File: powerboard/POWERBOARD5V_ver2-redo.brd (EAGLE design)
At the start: 42 x 70 mm, 37 parts, among them IC1 TPS5420, IC2 TPS5420

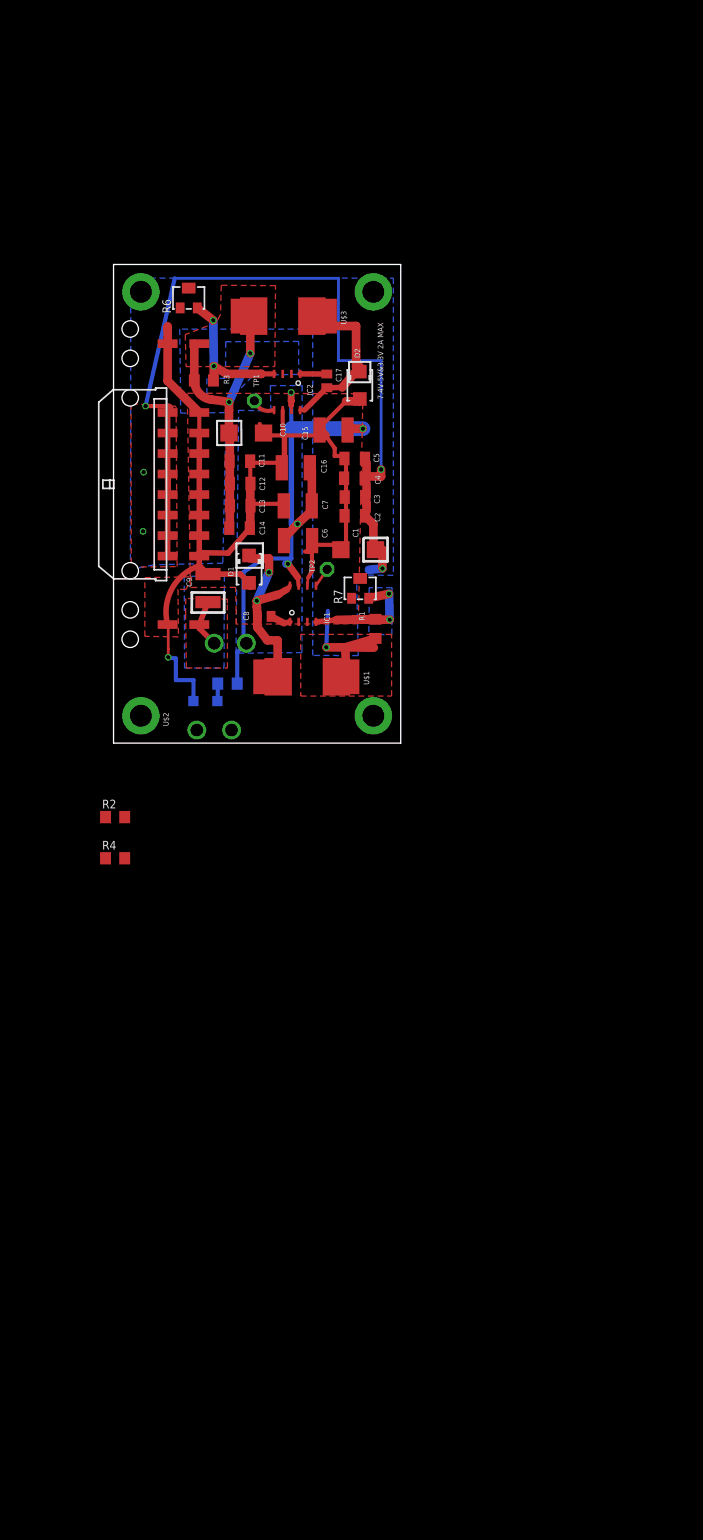
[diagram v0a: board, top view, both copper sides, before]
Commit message: Added the 6volt rail to schematic. Board not done.
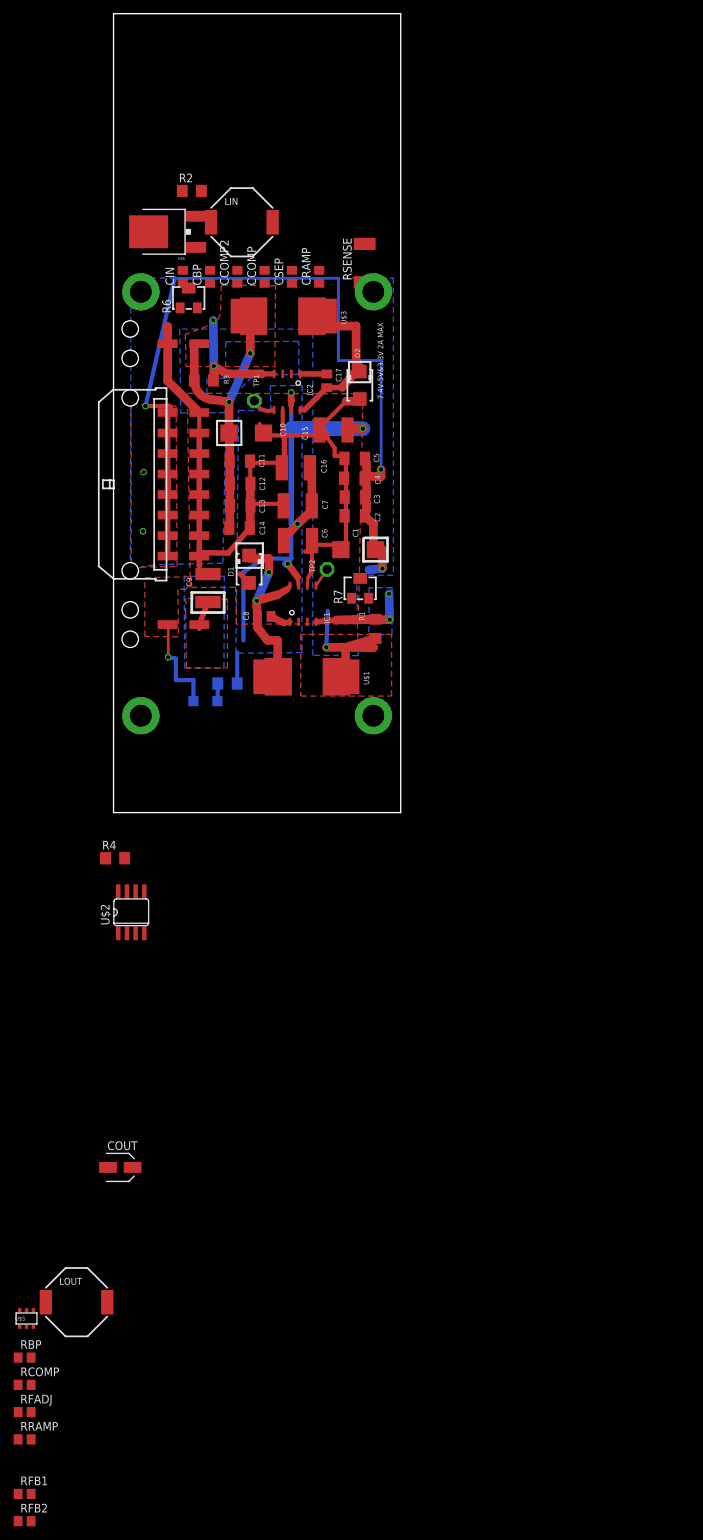
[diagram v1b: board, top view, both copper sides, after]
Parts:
- added CBP: 100nF, rcl:C0805
- added CCOMP: 120nF, rcl:C0805
- added CCOMP2: 510pF, rcl:C0805
- added CIN: 22uF, rcl:C0805
- added COUT: 56uF, rcl:SANYO-OSCON_SMD_A5
- added CRAMP: 750pF, rcl:C0805
- added CSEP: 2.2uF, rcl:C0805
- added LIN: 6.2uH, SparkFun-Passives:SRU1038
- added LOUT: 15uH, SparkFun-Passives:SRU1038
- added RBP: 20.0, rcl:R0805
- added RCOMP: 1.47k, rcl:R0805
- added RFADJ: 34.8k, rcl:R0805
- added RFB1: 10k, rcl:R0805
- added RFB2: 37.4k, rcl:R0805
- added RRAMP: 100.0, rcl:R0805
- added RSENSE: 0.016, rcl:R2512
- added U$5: P-CHANNEL20V(D-S)MOSFET, ngohara_parts:TSOP-6
- added U$6: DPAK_DIODE, ngohara_parts:DPAK
- U$2: value 90701WESWITCHDEV -> LM3488; device daniel:9070-1W-ESWITCH -> 40xx:SO08
- moved R2 92.3 mm to (11.5, 80.7)
- moved U$2 29.3 mm to (2.59, -24.7), turned to 0 degrees
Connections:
- net N$1 renamed 5V
- net N$9 renamed 3_3V
- removed net N$3: C15.1, C16.1, C6.1, C7.1, IC1.7, IC2.7, R5.1, U$2.1
- new net FB: RFB1.1, RFB2.2, U$2.3
- new net N$1: CCOMP.1, RCOMP.1
- new net N$20: RFADJ.2, U$2.7
- new net N$21: CRAMP.1, RRAMP.2, U$2.1
- new net N$22: RRAMP.1, RSENSE.2, U$5.P$1, U$5.P$2, U$5.P$5, U$5.P$6
- new net N$23: U$2.6, U$5.P$3
- new net N$24: CSEP.1, LIN.2, U$5.P$4
- new net N$25: CSEP.2, LOUT.1, U$6.1, U$6.3
- new net N$26: COUT.+, RFB2.1, U$6.4
- new net N$9: CBP.1, RBP.1, U$2.8
- new net V_BATT: C15.1, C16.1, C6.1, C7.1, C9.1, CIN.1, IC1.7, IC2.7, LIN.1, R5.1, RBP.2, X4.P$2
- net GND: now also CBP.2, CCOMP.2, CCOMP2.2, CIN.2, COUT.-, CRAMP.2, LOUT.2, RFADJ.1, RFB1.2, RSENSE.1, U$2.4, U$2.5
- net N$12: now also R6.2; no longer R6.3
- net N$5: now also R7.2; no longer R7.3
- net N$7: now also CCOMP2.1, RCOMP.2; no longer C9.1, X4.P$2
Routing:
- net V_BATT: track 0.00 -> 84.1 mm, vias 0 -> 4
- net N$3: track 82.0 -> 0.00 mm, vias 4 -> 0
- net GND: track 161.4 -> 144.8 mm
- net N$7: track 7.15 -> 0.00 mm
- net N$5: track 20.7 -> 17.7 mm
- net N$12: track 21.1 -> 18.1 mm
- added copper zone on layer 1, net V_BATT
- added copper zone on layer 16, net V_BATT
- removed copper zone on layer 1, net N$7
- removed copper zone on layer 16, net N$7
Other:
- board size 42 x 70 mm -> 42 x 116.8 mm

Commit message: Flipped board on side to fit within EagleLite's size limits
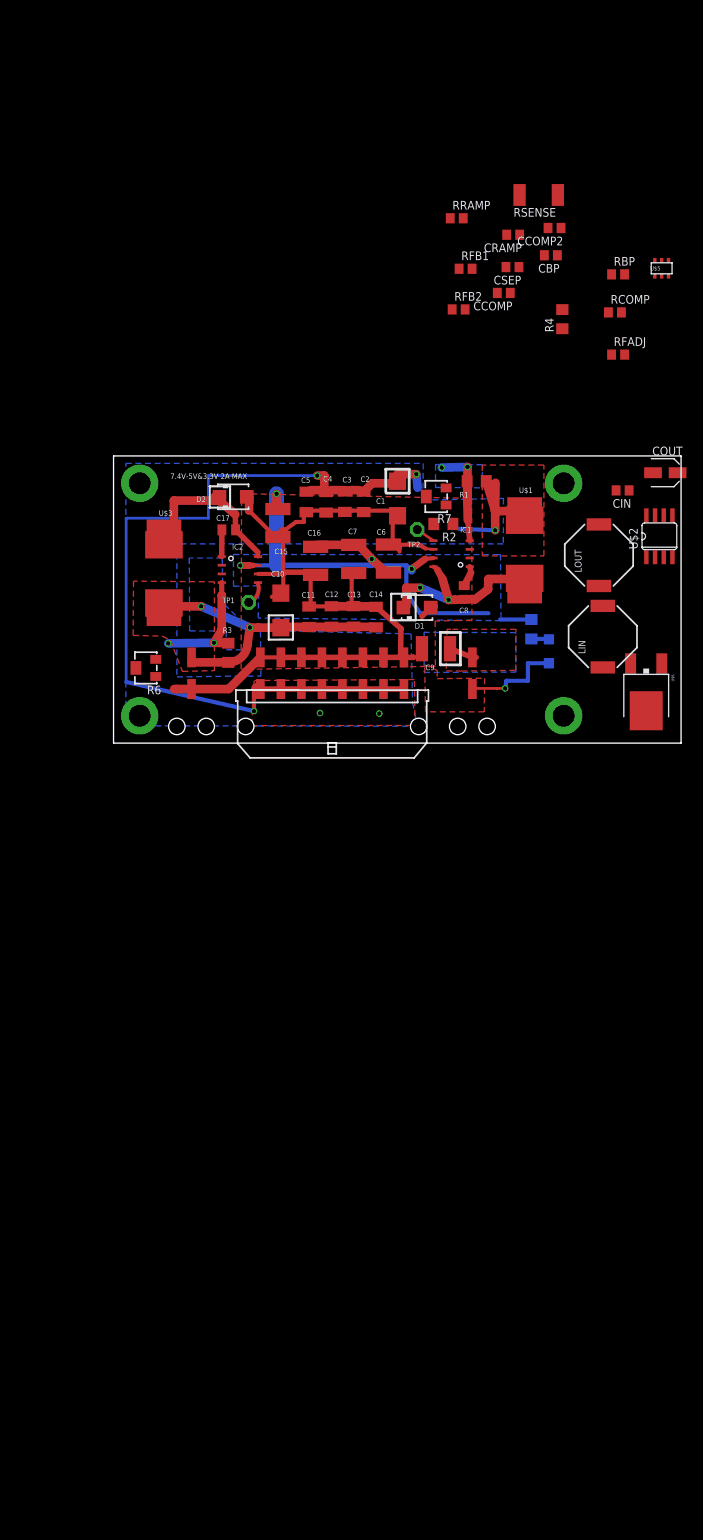
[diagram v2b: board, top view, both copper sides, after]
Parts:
- R2, R4: value 10.0k -> (none)
- moved RFB1 190.4 mm to (51.5, 69.4)
- moved RRAMP 189.4 mm to (50.2, 76.8)
- moved RFB2 188.2 mm to (50.5, 63.4)
- moved RBP 180.6 mm to (73.8, 68.6)
- moved U$5 179.5 mm to (80.2, 69.4)
- moved RCOMP 179.0 mm to (73.3, 63.0)
- moved RFADJ 177.3 mm to (73.8, 56.8)
- moved LOUT 133.3 mm to (71.0, 27.5), turned to 90 degrees
- moved COUT 129.1 mm to (80.7, 39.5)
- moved R4 102.4 mm to (65.6, 62.0), turned to 90 degrees
- moved U$6 98.7 mm to (77.9, 6.32), turned to 180 degrees
- moved U$2 94.8 mm to (79.8, 30.3)
- moved LIN 80.4 mm to (71.6, 15.6), turned to 90 degrees
- moved CIN 71.5 mm to (74.4, 37.0), turned to 180 degrees
- moved R2 61.0 mm to (48.2, 32.1), turned to 180 degrees
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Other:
- board size 42 x 116.8 mm -> 83 x 42 mm

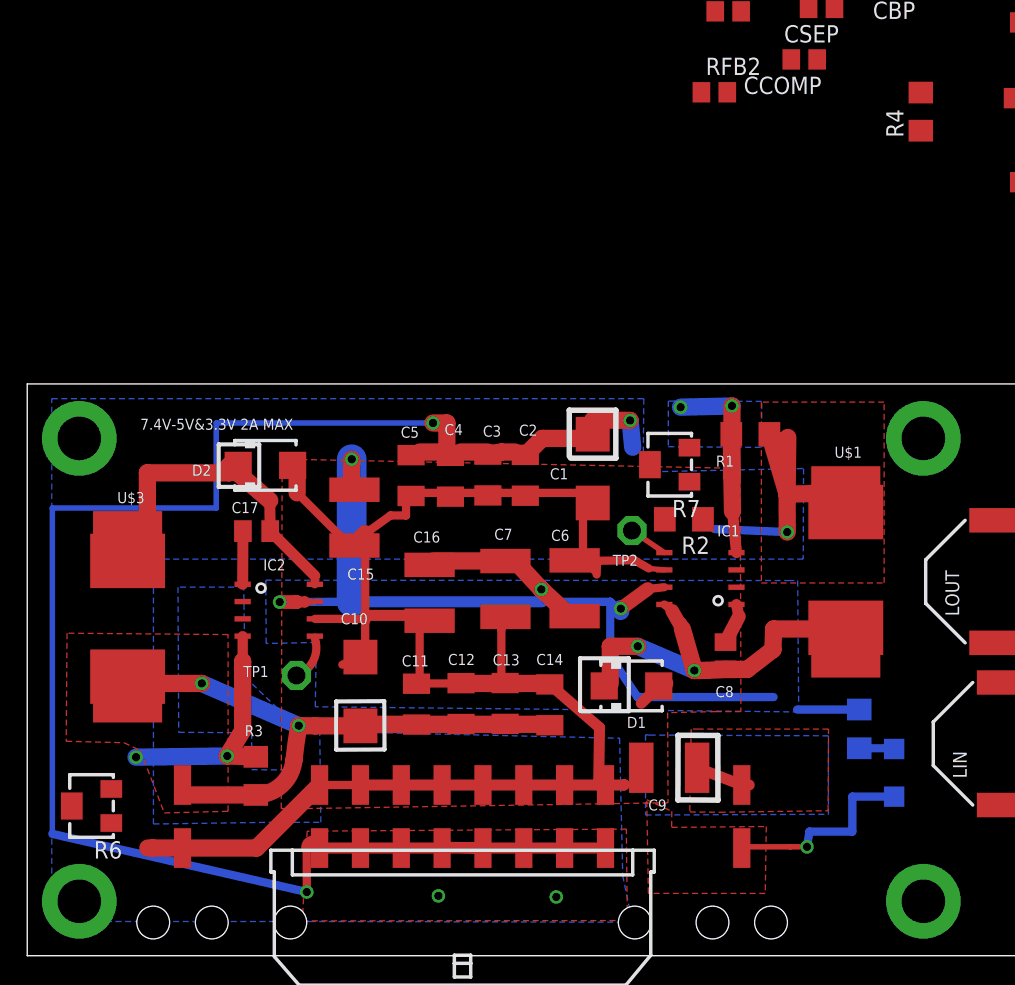
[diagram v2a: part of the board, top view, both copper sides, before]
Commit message: Deleted TP1 and TP2 (test points) because they seem useless
-Moved parts around to reduce footprint
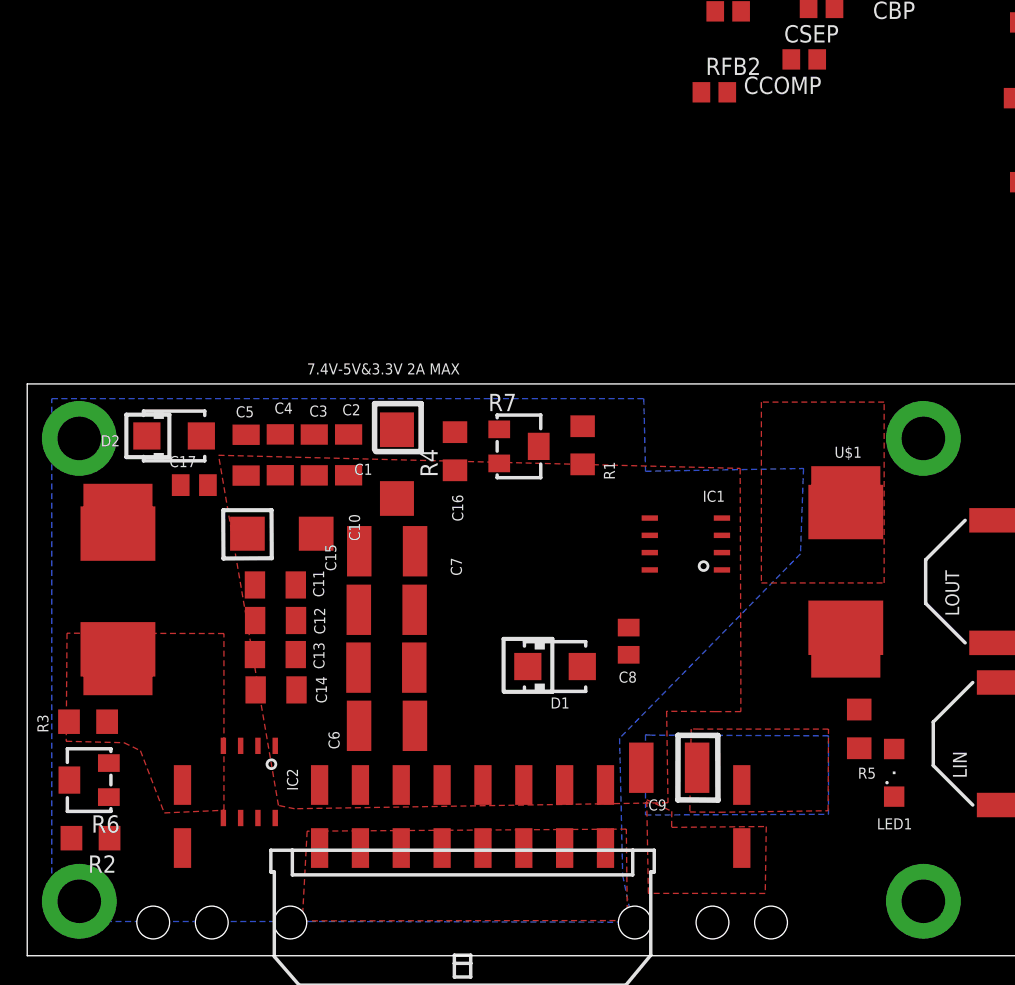
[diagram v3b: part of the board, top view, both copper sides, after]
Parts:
- removed TP1, TP2: PTR1PAD1-13, testpad:P1-13
- moved R2 49.5 mm to (4.65, 8.64)
- moved R4 42.3 mm to (31.4, 37.1)
- moved C14 20.1 mm to (18.3, 19.5), turned to 0 degrees
- moved C13 17.3 mm to (18.2, 22.1), turned to 0 degrees
- moved IC2 17.2 mm to (18.8, 10.8), turned to 180 degrees
- moved C6 17.1 mm to (26.4, 16.9), turned to 180 degrees
- moved C12 14.9 mm to (18.2, 24.6), turned to 0 degrees
- moved C1 14.4 mm to (27.2, 36.1)
- moved C11 13.6 mm to (18.2, 27.2), turned to 0 degrees
- moved C2 13.1 mm to (23.6, 36.8)
- moved C10 12.9 mm to (18.7, 31.0), turned to 180 degrees
- moved R3 12.9 mm to (4.47, 17.2), turned to 0 degrees
- moved C3 12.8 mm to (21.1, 36.8)
- moved C4 12.6 mm to (18.6, 36.8)
- moved R1 12.3 mm to (40.8, 37.5), turned to 90 degrees
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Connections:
- removed net N$4: IC2.5, TP1.TP
- removed net N$8: IC1.5, TP2.TP
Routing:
- net 5V: track 158.0 -> 0.00 mm, vias 6 -> 0
- net GND: track 144.8 -> 0.00 mm, vias 1 -> 0
- net V_BATT: track 84.1 -> 0.00 mm, vias 4 -> 0
- net 3_3V: track 46.3 -> 0.00 mm, vias 2 -> 0
- net N$6: track 32.5 -> 0.00 mm, vias 2 -> 0
- net N$13: track 29.4 -> 0.00 mm
- net N$12: track 18.1 -> 0.00 mm, vias 2 -> 0
- net N$5: track 17.7 -> 0.00 mm, vias 2 -> 0
- net N$10: track 3.91 -> 0.00 mm
- net N$4: track 3.20 -> 0.00 mm
- net N$2: track 3.02 -> 0.00 mm
- net N$8: track 2.88 -> 0.00 mm
- net N$17: track 2.59 -> 0.00 mm
- removed copper zone on layer 16, net 3_3V
- removed copper zone on layer 16, net N$3
- removed copper zone on layer 16, net N$5

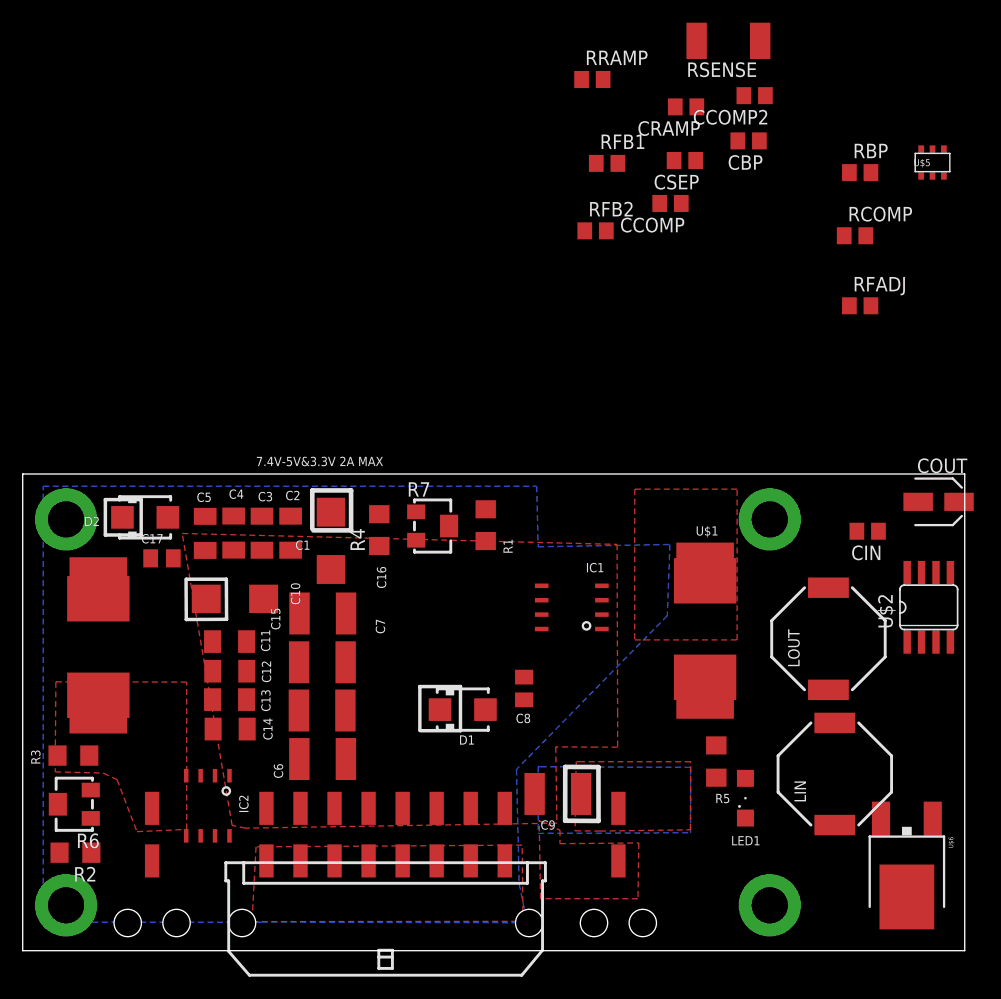
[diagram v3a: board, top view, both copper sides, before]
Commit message: Finished layout of power board with 6V.
-Does not include new connectors for 3.3 and 5v rail yet
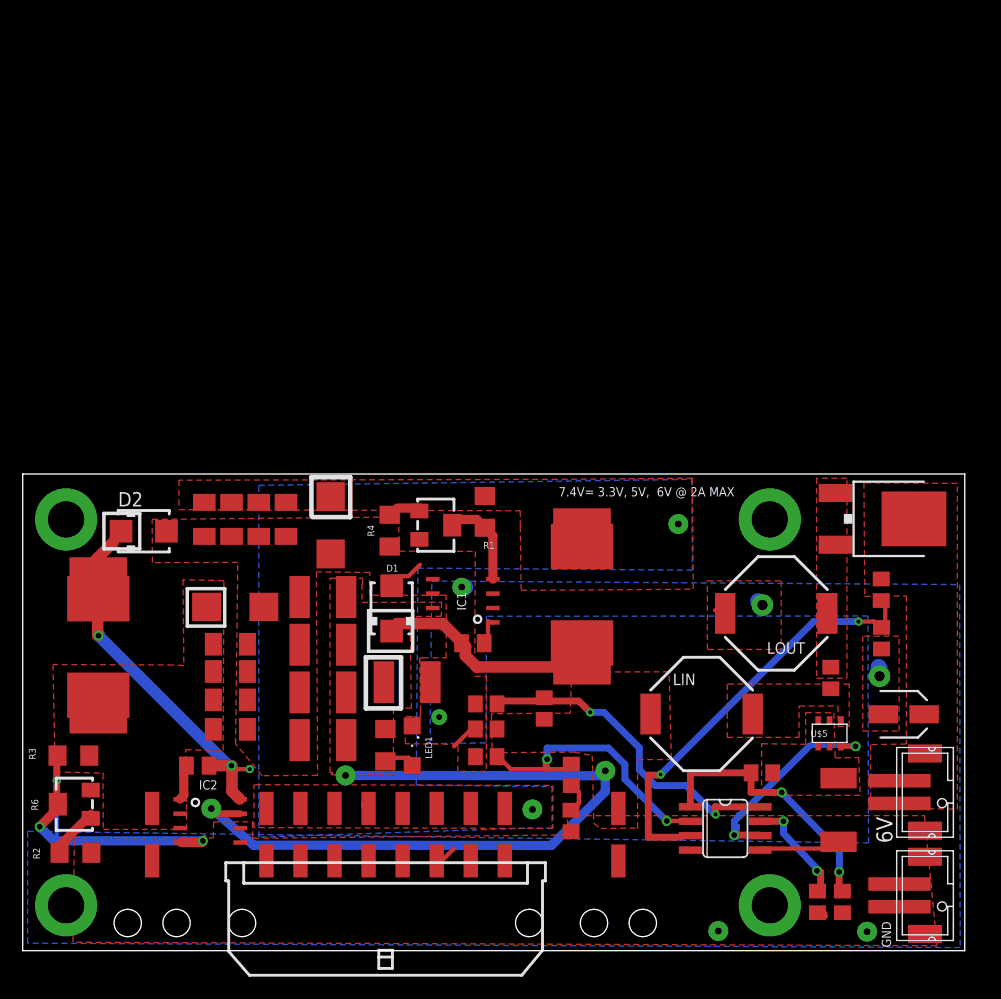
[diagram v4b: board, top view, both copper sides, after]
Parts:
- added U$4, U$7: JST-PH2-SMD, jst-ph:JST-PH2-SMD
- R5: value (none) -> 250
- moved CRAMP 71.4 mm to (72.2, 4.30), turned to 270 degrees
- moved RSENSE 68.5 mm to (71.9, 12.4), turned to 90 degrees
- moved RRAMP 62.9 mm to (65.1, 15.7), turned to 180 degrees
- moved CCOMP2 62.9 mm to (40.8, 17.1)
- moved CCOMP 55.1 mm to (48.3, 11.4), turned to 270 degrees
- moved RBP 54.8 mm to (45.9, 21.3), turned to 270 degrees
- moved CBP 54.7 mm to (40.8, 21.7)
- moved RCOMP 53.7 mm to (48.3, 15.5), turned to 90 degrees
- moved RFADJ 52.7 mm to (70.0, 4.30), turned to 90 degrees
- moved U$5 51.1 mm to (71.1, 19.2)
- moved RFB1 48.3 mm to (75.7, 27.5), turned to 270 degrees
- moved CSEP 47.4 mm to (71.2, 24.0), turned to 90 degrees
- moved RFB2 40.4 mm to (75.6, 31.8), turned to 270 degrees
- moved CIN 37.9 mm to (40.8, 19.5)
- moved U$6 31.7 mm to (76.9, 38.0), turned to 270 degrees
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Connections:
- net N$22 renamed SIG1
- net N$24 renamed LINSIG
- net N$25 renamed LSIG
- removed net N$26: COUT.+, RFB2.1, U$6.4
- new net 6V: COUT.+, RFB2.1, U$4.P$1, U$4.P$2, U$6.4
- net 5V: now also X1.P$10, X1.P$11, X1.P$12, X1.P$13, X1.P$14, X1.P$15, X1.P$16, X1.P$9; no longer X1.P$1, X1.P$2, X1.P$3, X1.P$4, X1.P$5, X1.P$6, X1.P$7, X1.P$8
- net GND: now also U$7.P$1, U$7.P$2, X1.P$1, X1.P$2, X1.P$3, X1.P$4, X1.P$5, X1.P$6, X1.P$7, X1.P$8; no longer X1.P$10, X1.P$11, X1.P$12, X1.P$13, X1.P$14, X1.P$15, X1.P$16, X1.P$9
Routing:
- net V_BATT: track 0.00 -> 66.1 mm, vias 0 -> 3
- net N$13: track 0.00 -> 38.8 mm, vias 0 -> 3
- net FB: track 0.00 -> 38.6 mm, vias 0 -> 2
- net N$12: track 0.00 -> 31.1 mm, vias 0 -> 3
- net N$9: track 0.00 -> 29.6 mm, vias 0 -> 2
- net GND: track 0.00 -> 28.4 mm, vias 0 -> 6
- net N$3: track 0.00 -> 26.2 mm, vias 0 -> 2
- net N$21: track 0.00 -> 24.1 mm, vias 0 -> 2
- net N$6: track 0.00 -> 22.4 mm
- net N$23: track 0.00 -> 20.6 mm, vias 0 -> 2
- net N$20: track 0.00 -> 10.4 mm, vias 0 -> 2
- net N$5: track 0.00 -> 8.38 mm
- net N$18: track 0.00 -> 5.03 mm
- net N$10: track 0.00 -> 3.70 mm
- net N$19: track 0.00 -> 3.16 mm
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- added copper zone on layer 1, net 6V
- added copper zone on layer 16, net GND
- added copper zone on layer 1, net LINSIG
- added copper zone on layer 1, net LSIG
- added copper zone on layer 1, net SIG1
- removed copper zone on layer 16, net V_BATT
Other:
- board text added: "6V"
- board text added: "7.4V= 3.3V, 5V, 6V @ 2A MAX"
- board text added: "GND"
- board text added: "REV. June 23 2013"
- board text added: "Wolfbot Swarm Robotics"
- board text removed: "7.4V-5V&3.3V 2A MAX"
- board text removed: "POWER BOARD"
- board text removed: "REV. F"
- board text removed: "Senior Design 11"
- board text removed: "Swarm Robotics"
